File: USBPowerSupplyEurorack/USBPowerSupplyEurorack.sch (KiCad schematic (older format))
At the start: 19 parts, among them J1 1734366-1, J2 10129381-910001BLF, Q1 Q_PMOS_GSD

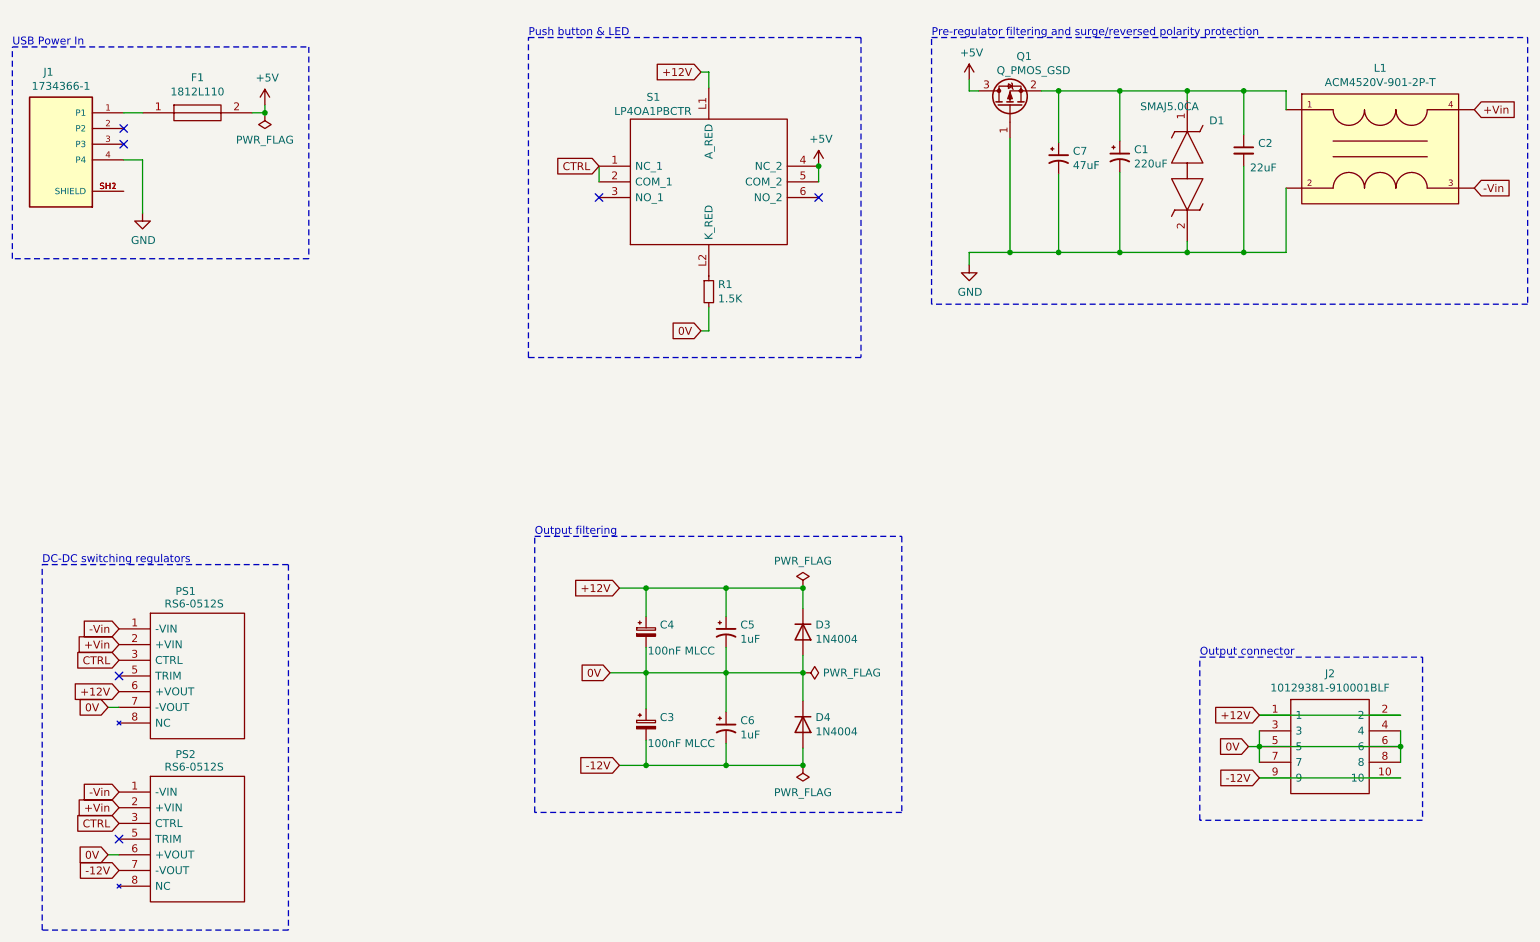
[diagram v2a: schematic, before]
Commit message: finished updating footprints, edited TVS diode's footprint
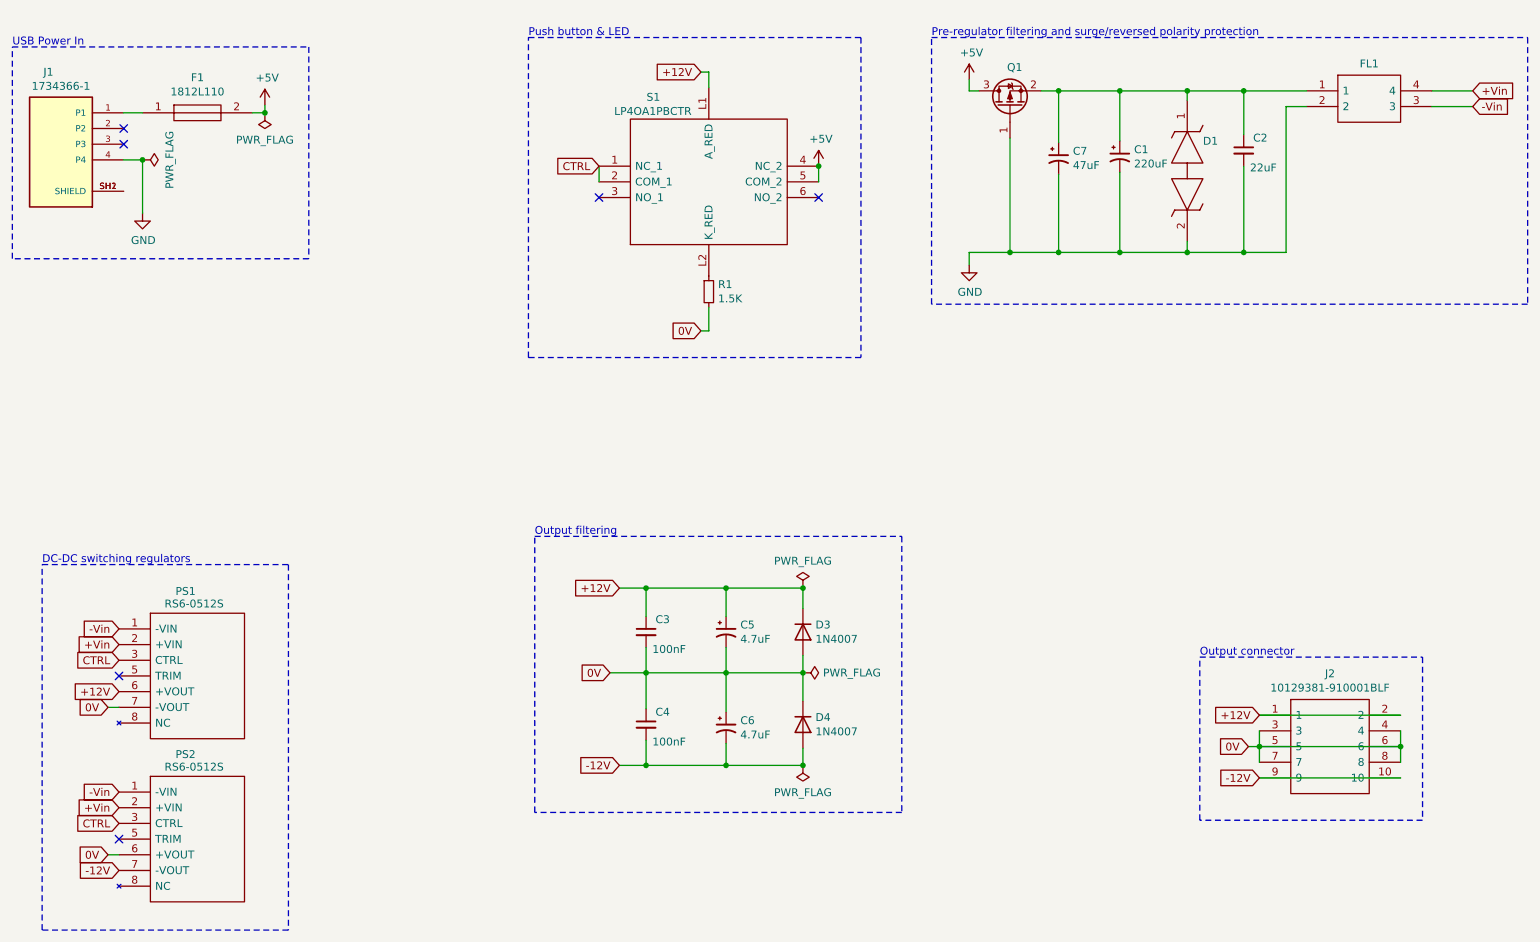
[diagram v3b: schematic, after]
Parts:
- removed C3, C4: 100nF MLCC, Capacitor_SMD:C_1206_3216Metric, symbol Device:CP_Small
- removed L1: ACM4520V-901-2P-T, eec2:TDK-ACM4520V-901-2P-T-0, symbol eec2:ACM4520V-901-2P-T
- added C3, C4: 100nF, Capacitor_SMD:C_0402_1005Metric, symbol Device:C_Small
- added FL1: ACP3225-102-2P-T000, ACP3225-102-2P-T000:ACP3225, symbol ACP3225-102-2P-T000:ACP3225-102-2P-T000
- C5, C6: value 1uF -> 4.7uF; LCSC (none) -> C116398
- D1: footprint digikey-footprints:DO-214AC -> digikey-footprints:DO-214AC-BIPOLAR
- D3, D4: value 1N4004 -> 1N4007; LCSC (none) -> C64898
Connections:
- net +12V: now also C3.1
- net +Vin: now also FL1.4
- net -12V: now also C4.2
- net -Vin: now also FL1.3
- net 0V: now also C3.2, C4.1
- net GND: now also FL1.2
- net at C1.1, C2.1, C7.1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: now also FL1.1
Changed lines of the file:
@@
 	2560 1490 2560 1440
 Connection ~ 8010 1350
-Text GLabel 10270 1470 2    50   Input ~ 0
+Text GLabel 10260 1350 2    50   Input ~ 0
 +Vin
-Text GLabel 10270 1970 2    50   Input ~ 0
+Text GLabel 10260 1450 2    50   Input ~ 0
 -Vin
-$Comp
-L Device:CP_Small C3
-U 1 1 5FE49BEB
-P 4990 5390
-F 0 "C3" H 5078 5436 50  0000 L CNN
-F 1 "100nF MLCC" H 5000 5270 50  0000 L CNN
-F 2 "Capacitor_SMD:C_1206_3216Metric" H 4990 5390 50  0001 C CNN
-F 3 "~" H 4990 5390 50  0001 C CNN
-	1    4990 5390
-	1    0    0    -1
-$EndComp
 $Comp
 L Device:CP1_Small C7
@@
 P 5990 4800
 F 0 "D3" V 5944 4880 50  0000 L CNN
-F 1 "1N4004" V 6035 4880 50  0000 L CNN
+F 1 "1N4007" V 6035 4880 50  0000 L CNN
 F 2 "Diode_SMD:D_SOD-123F" H 5990 4625 50  0001 C CNN
 F 3 "http://www.vishay.com/docs/88503/1n4001.pdf" H 5990 4800 50  0001 C CNN
+F 4 "C64898" H 5990 4800 50  0001 C CNN "LCSC"
 	1    5990 4800
 	0    1    1    0
-$EndComp
-$Comp
-L Device:CP_Small C4
-U 1 1 5FE6E630
-P 4990 4800
-F 0 "C4" H 5078 4846 50  0000 L CNN
-F 1 "100nF MLCC" H 5000 4680 50  0000 L CNN
-F 2 "Capacitor_SMD:C_1206_3216Metric" H 4990 4800 50  0001 C CNN
-F 3 "~" H 4990 4800 50  0001 C CNN
-	1    4990 4800
-	1    0    0    -1
 $EndComp
 Wire Wire Line
@@
 P 5500 4800
 F 0 "C5" H 5591 4846 50  0000 L CNN
-F 1 "1uF" H 5591 4755 50  0000 L CNN
+F 1 "4.7uF" H 5591 4755 50  0000 L CNN
 F 2 "Capacitor_SMD:C_Elec_4x5.4" H 5500 4800 50  0001 C CNN
 F 3 "~" H 5500 4800 50  0001 C CNN
+F 4 "C116398" H 5500 4800 50  0001 C CNN "LCSC"
 	1    5500 4800
 	1    0    0    -1
@@
 P 5500 5410
 F 0 "C6" H 5591 5456 50  0000 L CNN
-F 1 "1uF" H 5591 5365 50  0000 L CNN
+F 1 "4.7uF" H 5591 5365 50  0000 L CNN
 F 2 "Capacitor_SMD:C_Elec_4x5.4" H 5500 5410 50  0001 C CNN
 F 3 "~" H 5500 5410 50  0001 C CNN
+F 4 "C116398" H 5500 5410 50  0001 C CNN "LCSC"
 	1    5500 5410
 	1    0    0    -1
@@
 P 5990 5390
 F 0 "D4" V 5944 5470 50  0000 L CNN
-F 1 "1N4004" V 6035 5470 50  0000 L CNN
+F 1 "1N4007" V 6035 5470 50  0000 L CNN
 F 2 "Diode_SMD:D_SOD-123F" H 5990 5215 50  0001 C CNN
 F 3 "http://www.vishay.com/docs/88503/1n4001.pdf" H 5990 5390 50  0001 C CNN
+F 4 "C64898" H 5990 5390 50  0001 C CNN "LCSC"
 	1    5990 5390
 	0    1    1    0
@@
 U 1 1 5FE39F03
 P 7310 1450
-F 0 "Q1" V 7630 1360 50  0000 C CNN
-F 1 "Q_PMOS_GSD" V 7540 1300 50  0000 C CNN
+F 0 "Q1" V 7560 1420 50  0000 C CNN
+F 1 "Q_PMOS_GSD" V 7540 1300 50  0001 C CNN
 F 2 "digikey-footprints:SOT-23-3" H 7510 1550 50  0001 C CNN
 F 3 "https://www.mouser.fr/datasheet/2/916/PMV240SP-1919536.pdf" H 7310 1450 50  0001 C CNN
@@
 	5390 1230 5390 1330
 $Comp
-L eec2:ACM4520V-901-2P-T L1
-U 1 1 5FE60CD9
-P 8970 1470
-F 0 "L1" H 9670 1735 50  0000 C CNN
-F 1 "ACM4520V-901-2P-T" H 9670 1644 50  0000 C CNN
-F 2 "eec2:TDK-ACM4520V-901-2P-T-0" H 8970 1870 50  0001 L CNN
-F 3 "http://nl.rs-online.com/webdocs/14e9/0900766b814e92ac.pdf" H 8970 1970 50  0001 L CNN
-F 4 "Fuse" H 8970 2070 50  0001 L CNN "category"
-F 5 "2 Line Common Mode Choke Surface Mount 900 Ohm @ 100MHz 1.2A DCR 60 mOhm" H 8970 2170 50  0001 L CNN "digikey description"
-F 6 "445-15677-1-ND" H 8970 2270 50  0001 L CNN "digikey part number"
-F 7 "yes" H 8970 2370 50  0001 L CNN "lead free"
-F 8 "40a722fe90742dbf" H 8970 2470 50  0001 L CNN "library id"
-F 9 "TDK" H 8970 2570 50  0001 L CNN "manufacturer"
-F 10 "810-ACM4520V9012PT00" H 8970 2670 50  0001 L CNN "mouser part number"
-F 11 "L1808" H 8970 2770 50  0001 L CNN "package"
-F 12 "yes" H 8970 2870 50  0001 L CNN "rohs"
-F 13 "+125°C" H 8970 2970 50  0001 L CNN "temperature range high"
-F 14 "-40°C" H 8970 3070 50  0001 L CNN "temperature range low"
-F 15 "50V" H 8970 3170 50  0001 L CNN "voltage"
-F 16 "C92126" H 8970 1470 50  0001 C CNN "LCSC"
-	1    8970 1470
-	1    0    0    -1
-$EndComp
-$Comp
 L SMAJ5.0CA:SMAJ5.0CA D1
 U 1 1 5FE50B9A
 P 8440 1410
-F 0 "D1" V 8570 1550 50  0000 L CNN
-F 1 "SMAJ5.0CA" V 8480 1110 50  0000 L CNN
-F 2 "digikey-footprints:DO-214AC" H 9040 1560 50  0001 L BNN
+F 0 "D1" V 8700 1510 50  0000 L CNN
+F 1 "SMAJ5.0CA" V 8480 1110 50  0001 L CNN
+F 2 "digikey-footprints:DO-214AC-BIPOLAR" H 9040 1560 50  0001 L BNN
 F 3 "http://www.littelfuse.com/~/media/electronics/datasheets/tvs_diodes/littelfuse_tvs_diode_smaj_datasheet.pdf.pdf" H 9040 1460 50  0001 L BNN
 F 4 "Littelfuse SMAJ5.0CA Bi-Directional TVS Diode, 400W peak, 2-Pin DO-214AC" H 9040 1360 50  0001 L BNN "Description"
@@
 	8800 1350 8800 1630
 Connection ~ 8440 1350
-Wire Wire Line
-	8800 1350 9070 1350
-Wire Wire Line
-	9070 1350 9070 1470
 Connection ~ 8800 1350
-Wire Wire Line
-	9070 2380 9070 1970
 Wire Wire Line
 	8800 1830 8800 2380
@@
 	8440 2380 8800 2380
 $Comp
-L power:+5V #PWR?
+L power:+5V #PWR0102
 U 1 1 5FE7630F
 P 2560 1440
-F 0 "#PWR?" H 2560 1290 50  0001 C CNN
+F 0 "#PWR0102" H 2560 1290 50  0001 C CNN
 F 1 "+5V" H 2575 1613 50  0000 C CNN
 F 2 "" H 2560 1440 50  0001 C CNN
@@
 U 1 1 5FEA4264
 P 8800 1730
-F 0 "C2" H 8892 1776 50  0000 L CNN
+F 0 "C2" H 8860 1810 50  0000 L CNN
 F 1 "22uF" H 8840 1620 50  0000 L CNN
 F 2 "Capacitor_SMD:C_0805_2012Metric" H 8800 1730 50  0001 C CNN
@@
 	1    0    0    -1
 $EndComp
+$Comp
+L ACP3225-102-2P-T000:ACP3225-102-2P-T000 FL1
+U 1 1 5FEA5D5D
+P 9200 1350
+F 0 "FL1" H 9600 1523 50  0000 C CNN
+F 1 "ACP3225-102-2P-T000" H 9600 1524 50  0001 C CNN
+F 2 "ACP3225-102-2P-T000:ACP3225" H 9850 1450 50  0001 L CNN
+F 3 "https://componentsearchengine.com/Datasheets/2/ACP3225-102-2P-T000.pdf" H 9850 1350 50  0001 L CNN
+F 4 "Common Mode Choke 1kR 1,2A R1 SMD TDK ACP Series Shielded SMD Common Mode Line Filter 1.5A Idc" H 9850 1250 50  0001 L CNN "Description"
+F 5 "" H 9850 1150 50  0001 L CNN "Height"
+F 6 "TDK" H 9850 1050 50  0001 L CNN "Manufacturer_Name"
+F 7 "ACP3225-102-2P-T000" H 9850 950 50  0001 L CNN "Manufacturer_Part_Number"
+F 8 "810-ACP32251022PT000" H 9850 850 50  0001 L CNN "Mouser Part Number"
+F 9 "https://www.mouser.co.uk/ProductDetail/TDK/ACP3225-102-2P-T000/?qs=ivTIEzcXi434Fc9I%252Be4KYw%3D%3D" H 9850 750 50  0001 L CNN "Mouser Price/Stock"
+F 10 "ACP3225-102-2P-T000" H 9850 650 50  0001 L CNN "Arrow Part Number"
+F 11 "https://www.arrow.com/en/products/acp3225-102-2p-t000/tdk" H 9850 550 50  0001 L CNN "Arrow Price/Stock"
+F 12 "C92126" H 9200 1350 50  0001 C CNN "LCSC"
+	1    9200 1350
+	1    0    0    -1
+$EndComp
+Wire Wire Line
+	8800 1350 9200 1350
+Wire Wire Line
+	9070 1450 9200 1450
+Wire Wire Line
+	9070 1450 9070 2380
+Wire Wire Line
+	10000 1350 10260 1350
+Wire Wire Line
+	10000 1450 10260 1450
+$Comp
+L Device:C_Small C3
+U 1 1 5FEB06CB
+P 4990 4800
+F 0 "C3" H 5050 4880 50  0000 L CNN
+F 1 "100nF" H 5030 4690 50  0000 L CNN
+F 2 "Capacitor_SMD:C_0402_1005Metric" H 4990 4800 50  0001 C CNN
+F 3 "~" H 4990 4800 50  0001 C CNN
+F 4 "C1525" H 4990 4800 50  0001 C CNN "LCSC"
+	1    4990 4800
+	1    0    0    -1
+$EndComp
+$Comp
+L Device:C_Small C4
+U 1 1 5FEB46EE
+P 4990 5390
+F 0 "C4" H 5050 5470 50  0000 L CNN
+F 1 "100nF" H 5030 5280 50  0000 L CNN
+F 2 "Capacitor_SMD:C_0402_1005Metric" H 4990 5390 50  0001 C CNN
+F 3 "~" H 4990 5390 50  0001 C CNN
+F 4 "C1525" H 4990 5390 50  0001 C CNN "LCSC"
+	1    4990 5390
+	1    0    0    -1
+$EndComp
+$Comp
+L power:PWR_FLAG #FLG0104
+U 1 1 5FEB767D
+P 1780 1790
+F 0 "#FLG0104" H 1780 1865 50  0001 C CNN
+F 1 "PWR_FLAG" H 1780 1963 50  0000 C CNN
+F 2 "" H 1780 1790 50  0001 C CNN
+F 3 "~" H 1780 1790 50  0001 C CNN
+	1    1780 1790
+	0    1    1    0
+$EndComp
+Connection ~ 1780 1790
 $EndSCHEMATC

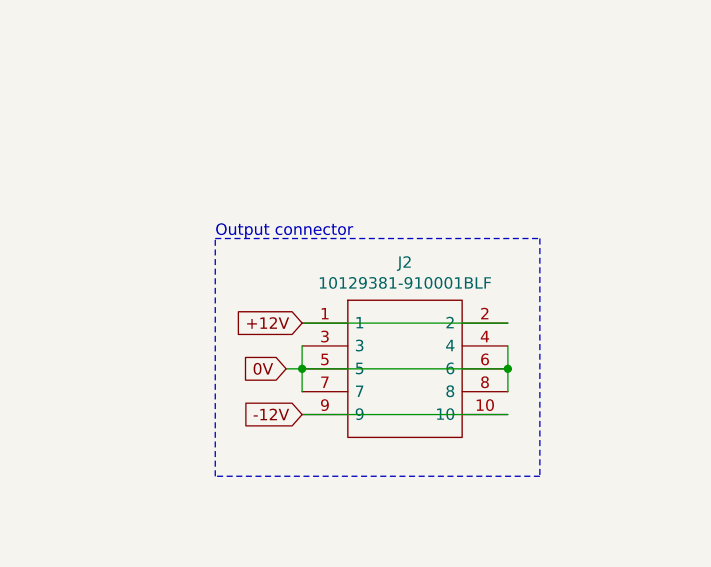
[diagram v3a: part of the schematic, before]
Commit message: replaced power header for SMT, finished placement
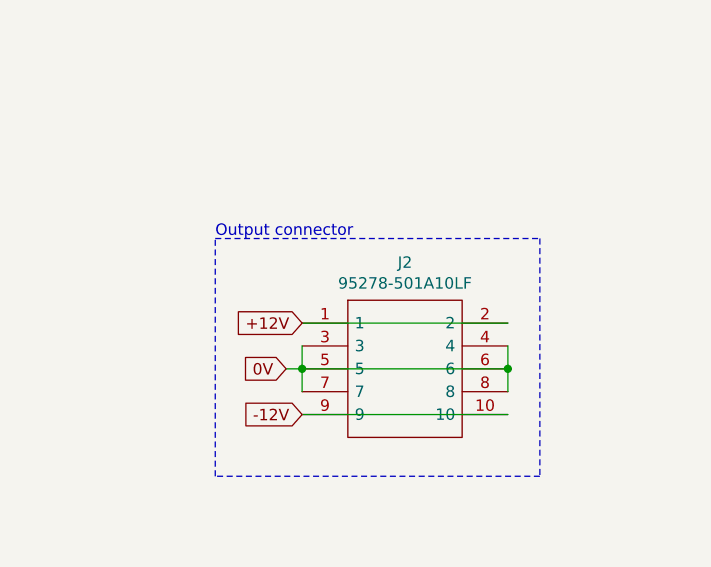
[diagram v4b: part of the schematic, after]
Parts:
- removed J2: 10129381-910001BLF, 10129381-910001BLF:HDRV10W67P254_2X5_1270X483X858P, symbol 10129381-910001BLF:10129381-910001BLF
- added J2: 95278-501A10LF, 95278-501A10LF:95278501A10LF, symbol 95278-501A10LF:95278-501A10LF
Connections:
- net +12V: now also J2.1, J2.2
- net -12V: now also J2.10, J2.9
- net 0V: now also J2.3, J2.4, J2.5, J2.6, J2.7, J2.8
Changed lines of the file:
@@
 Text GLabel 4820 4520 0    50   Input ~ 0
 +12V
-$Comp
-L 10129381-910001BLF:10129381-910001BLF J2
-U 1 1 5FE8C505
-P 8900 5330
-F 0 "J2" H 9350 5595 50  0000 C CNN
-F 1 "10129381-910001BLF" H 9350 5504 50  0000 C CNN
-F 2 "10129381-910001BLF:HDRV10W67P254_2X5_1270X483X858P" H 9650 5430 50  0001 L CNN
-F 3 "https://cdn.amphenol-icc.com/media/wysiwyg/files/drawing/10129381.pdf" H 9650 5330 50  0001 L CNN
-F 4 "EconoStik , Board to Board connector, Unshrouded Vertical Header, Through Hole, Double Row, 10 Positions, 2.54 mm (0.100in) Pitch" H 9650 5230 50  0001 L CNN "Description"
-F 5 "8.58" H 9650 5130 50  0001 L CNN "Height"
-F 6 "Amphenol" H 9650 5030 50  0001 L CNN "Manufacturer_Name"
-F 7 "10129381-910001BLF" H 9650 4930 50  0001 L CNN "Manufacturer_Part_Number"
-F 8 "649-1012938191001BLF" H 9650 4830 50  0001 L CNN "Mouser Part Number"
-F 9 "https://www.mouser.co.uk/ProductDetail/Amphenol-FCI/10129381-910001BLF?qs=0lQeLiL1qyYhmE%2FYsfo%2FnQ%3D%3D" H 9650 4730 50  0001 L CNN "Mouser Price/Stock"
-F 10 "10129381-910001BLF" H 9650 4630 50  0001 L CNN "Arrow Part Number"
-F 11 "https://www.arrow.com/en/products/10129381-910001blf/amphenol-fci" H 9650 4530 50  0001 L CNN "Arrow Price/Stock"
-	1    8900 5330
-	1    0    0    -1
-$EndComp
 Text GLabel 5340 2880 0    50   Input ~ 0
 0V
@@
 $EndComp
 Connection ~ 1780 1790
+$Comp
+L 95278-501A10LF:95278-501A10LF J2
+U 1 1 5FEC1F9A
+P 8900 5330
+F 0 "J2" H 9350 5595 50  0000 C CNN
+F 1 "95278-501A10LF" H 9350 5504 50  0000 C CNN
+F 2 "95278-501A10LF:95278501A10LF" H 9650 5430 50  0001 L CNN
+F 3 "https://componentsearchengine.com/Datasheets/1/95278-501A10LF.pdf" H 9650 5330 50  0001 L CNN
+F 4 "Headers & Wire Housings BERGSTIK" H 9650 5230 50  0001 L CNN "Description"
+F 5 "8.77" H 9650 5130 50  0001 L CNN "Height"
+F 6 "Amphenol" H 9650 5030 50  0001 L CNN "Manufacturer_Name"
+F 7 "95278-501A10LF" H 9650 4930 50  0001 L CNN "Manufacturer_Part_Number"
+F 8 "649-95278-501A10LF" H 9650 4830 50  0001 L CNN "Mouser Part Number"
+F 9 "https://www.mouser.com/Search/Refine.aspx?Keyword=649-95278-501A10LF" H 9650 4730 50  0001 L CNN "Mouser Price/Stock"
+F 10 "" H 9650 4630 50  0001 L CNN "Arrow Part Number"
+F 11 "" H 9650 4530 50  0001 L CNN "Arrow Price/Stock"
+	1    8900 5330
+	1    0    0    -1
+$EndComp
 $EndSCHEMATC
